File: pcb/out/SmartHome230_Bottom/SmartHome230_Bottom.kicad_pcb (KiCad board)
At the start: 2 copper layers, 120 x 92 mm, 58 parts, among them J1 B2B, J2 12V, J3 Przyciski A, J4 Przyciski B, J5 UART, J6 230V IN, J7 Wyj.1, J8 Wyj.2, K1 SRD-12V, K2 SRD-12V, Q1 BC547, Q2 BC547, SW1 EN, SW2 BOOT, U1 MP1584, U2 AMS1117-3.3, U3 ESP32-WROOM-32

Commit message: Zlicuj zlacza krawedziowe (bez zygzakow) + orientacja wejsciem do krawedzi
_place_row: zlacza I/O zlicowane zewnetrzna krawedzia ciala do brzegu plytki
(gorna krawedz rot 0, dolna strefa 230V rot 180) zamiast centrowania w pasie -
usuwa zygzaki przy krawedziach. Wnetrze (logika) nie wchodzi w pasy krawedziowe.

Co-Authored-By: Claude Opus 4.8 (1M context) <noreply@anthropic.com>
Claude-Session: https://claude.ai/code/session_01LNGxtK2Jv1rJLBLPTwFQ9C
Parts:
- moved J5 5.73 mm to (98.0, 3.27)
- moved J2 3.46 mm to (19.5, 5.54)
- moved J6 3.46 mm to (15.7, 86.5), turned to 180 degrees
- moved J7 3.46 mm to (83.5, 86.5), turned to 180 degrees
- moved J8 3.46 mm to (104.3, 86.5), turned to 180 degrees
- moved J3 2.50 mm to (44.0, 11.5)
- moved J4 2.50 mm to (70.9, 11.5)
- turned K1 to 180 degrees
- turned K2 to 180 degrees
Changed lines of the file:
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@@
     "pcbforge:ScrewTerminal_1x02_P5.08mm"
     (layer "F.Cu")
-    (at 19.5 9)
+    (at 19.5 5.54)
     (descr "Listwa zaciskowa 2x5.08mm")
     (attr through_hole)
@@
     "pcbforge:RJ45_8P8C"
     (layer "F.Cu")
-    (at 44 9)
+    (at 44 11.5)
     (descr "Gniazdo RJ45 8P8C THT")
     (attr through_hole)
@@
     "pcbforge:RJ45_8P8C"
     (layer "F.Cu")
-    (at 70.92 9)
+    (at 70.92 11.5)
     (descr "Gniazdo RJ45 8P8C THT")
     (attr through_hole)
@@
     "pcbforge:PinHeader_1x06_P2.54mm"
     (layer "F.Cu")
-    (at 97.96 9)
+    (at 97.96 3.27)
     (descr "Pin header 1x6")
     (attr through_hole)
@@
     "pcbforge:ScrewTerminal_1x03_P5.08mm"
     (layer "F.Cu")
-    (at 15.67 83)
+    (at 15.67 86.46 180)
     (descr "Listwa zaciskowa 3x5.08mm")
     (attr through_hole)
@@
     "pcbforge:Relay_SPDT_SRD"
     (layer "F.Cu")
-    (at 37.83 83)
+    (at 37.83 83 180)
     (descr "Przekaznik SRD SPDT (cewka + kontakty 230V)")
     (attr through_hole)
@@
     "pcbforge:Relay_SPDT_SRD"
     (layer "F.Cu")
-    (at 61.38 83)
+    (at 61.38 83 180)
     (descr "Przekaznik SRD SPDT (cewka + kontakty 230V)")
     (attr through_hole)
@@
     "pcbforge:ScrewTerminal_1x03_P5.08mm"
     (layer "F.Cu")
-    (at 83.55 83)
+    (at 83.55 86.46 180)
     (descr "Listwa zaciskowa 3x5.08mm")
     (attr through_hole)
@@
     "pcbforge:ScrewTerminal_1x03_P5.08mm"
     (layer "F.Cu")
-    (at 104.33 83)
+    (at 104.33 86.46 180)
     (descr "Listwa zaciskowa 3x5.08mm")
     (attr through_hole)

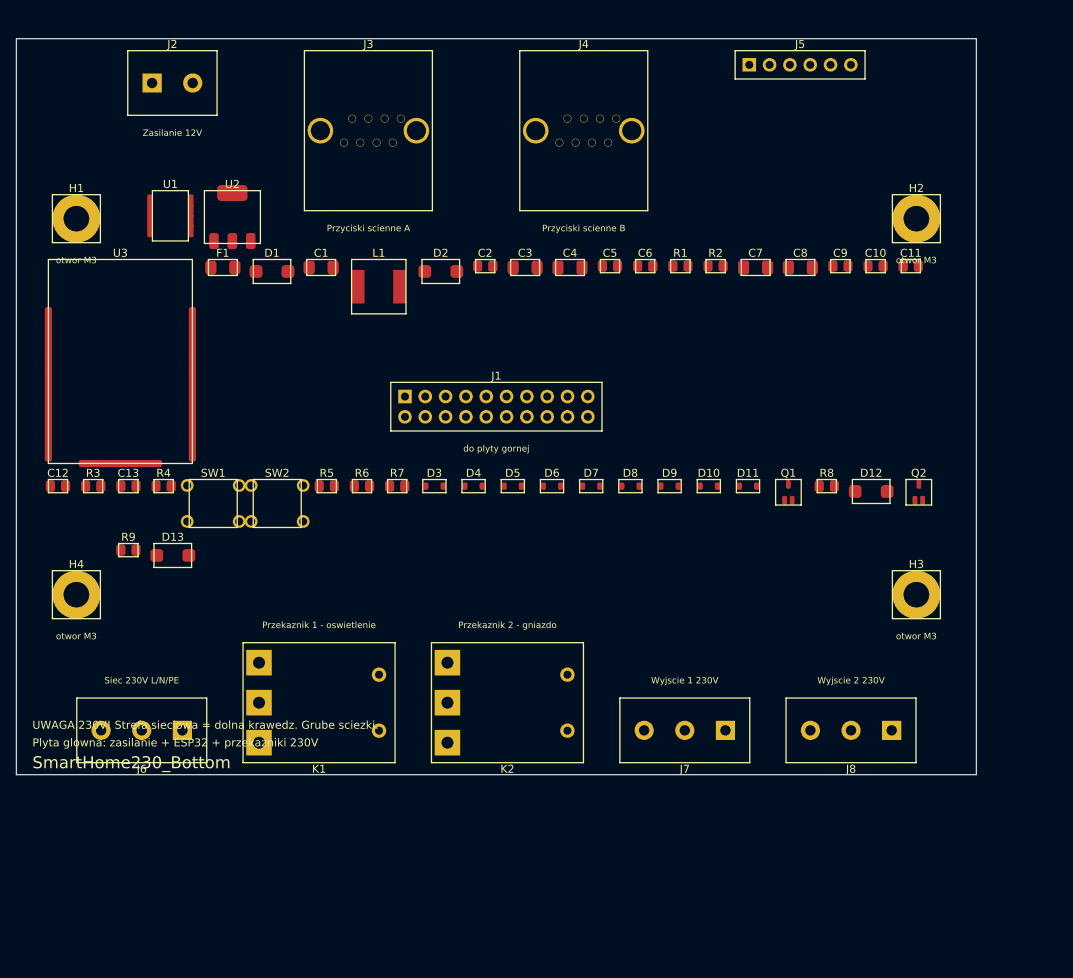
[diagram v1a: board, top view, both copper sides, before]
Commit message: Przekazniki do wnetrza (nie przy krawedzi); zaciski 230V zostaja na krawedzi
Rozdzielenie strefy 230V: zaciski sieciowe (dostep kablem) zlicowane przy dolnej
krawedzi, a przekazniki przeniesione do wnetrza w pas tuz nad zaciskami - z dala
od brzegu plytki (kolizja z obudowa). Logika pakowana nad strefa przekaznikow.
Powiekszona wspolna ramka (130x115) jako stala FRAME. SmartHome230 0/0/0, 11/11.

Co-Authored-By: Claude Opus 4.8 (1M context) <noreply@anthropic.com>
Claude-Session: https://claude.ai/code/session_01LNGxtK2Jv1rJLBLPTwFQ9C
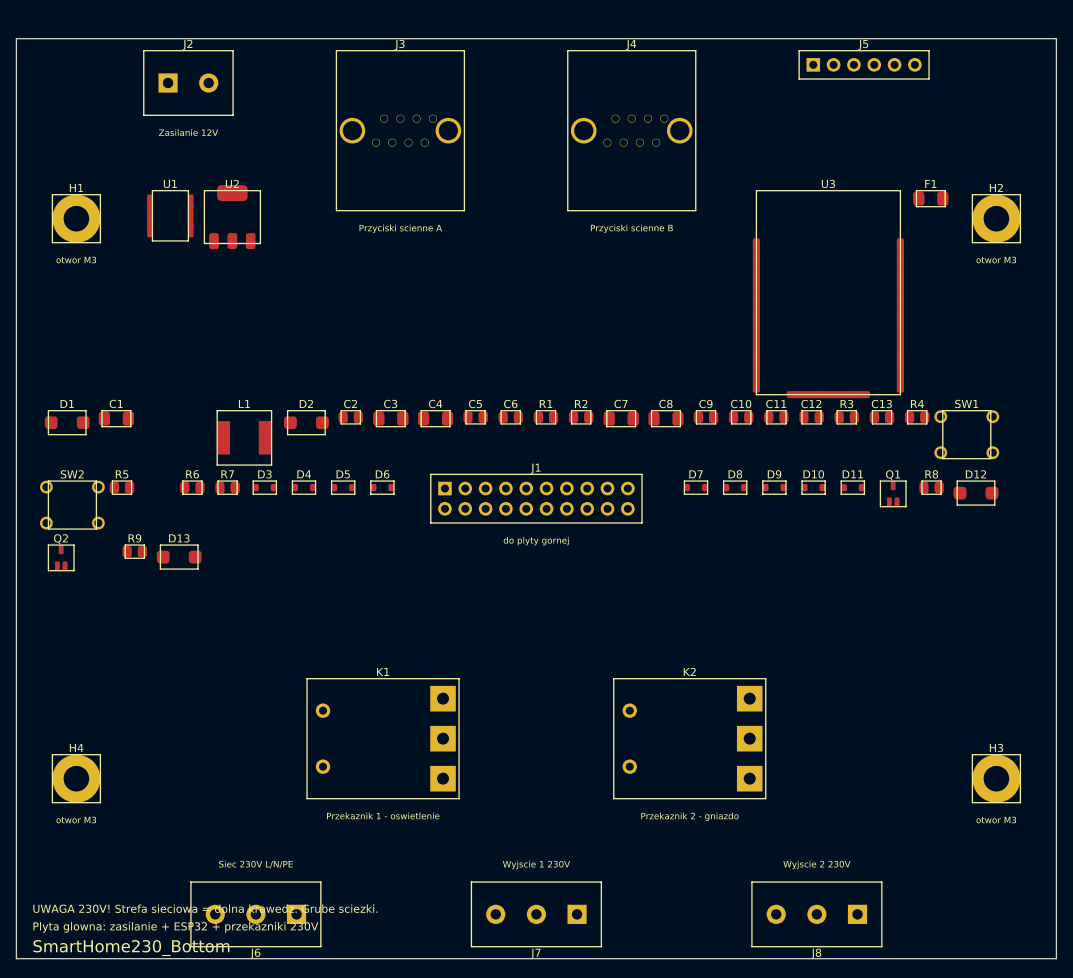
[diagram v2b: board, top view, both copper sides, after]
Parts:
- moved Q2 107.5 mm to (5.60, 64.9)
- moved C12 94.6 mm to (99.4, 47.3)
- moved C13 94.6 mm to (108.2, 47.3)
- moved R3 94.6 mm to (103.8, 47.3)
- moved R4 94.6 mm to (112.6, 47.3)
- moved SW1 94.6 mm to (118.8, 49.5)
- moved F1 88.9 mm to (114.3, 20.0)
- moved U3 88.9 mm to (101.5, 31.8)
- moved C1 31.8 mm to (12.5, 47.5)
- moved D1 31.8 mm to (6.35, 48.0)
- moved J7 29.5 mm to (65.0, 109.5)
- moved J6 27.1 mm to (29.9, 109.5)
- moved SW2 25.6 mm to (7.00, 58.3)
- moved R5 25.6 mm to (13.2, 56.1)
- moved C10 25.3 mm to (90.6, 47.3)
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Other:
- board size 120 x 92 mm -> 130 x 115 mm
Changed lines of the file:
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@@
     "pcbforge:MountingHole_M3"
     (layer "F.Cu")
-    (at 112.5 22.5)
+    (at 122.5 22.5)
     (descr "Otwor montazowy M3")
     (attr through_hole)
@@
     "pcbforge:MountingHole_M3"
     (layer "F.Cu")
-    (at 112.5 69.5)
+    (at 122.5 92.5)
     (descr "Otwor montazowy M3")
     (attr through_hole)
@@
     "pcbforge:MountingHole_M3"
     (layer "F.Cu")
-    (at 7.5 69.5)
+    (at 7.5 92.5)
     (descr "Otwor montazowy M3")
     (attr through_hole)
@@
     "pcbforge:PinHeader_2x10_P2.54mm"
     (layer "F.Cu")
-    (at 60 46)
+    (at 65 57.5)
     (descr "Pin header 2x10")
     (attr through_hole)
@@
     "pcbforge:ScrewTerminal_1x02_P5.08mm"
     (layer "F.Cu")
-    (at 19.5 5.54)
+    (at 21.5 5.54)
     (descr "Listwa zaciskowa 2x5.08mm")
     (attr through_hole)
@@
     "pcbforge:RJ45_8P8C"
     (layer "F.Cu")
-    (at 44 11.5)
+    (at 48 11.5)
     (descr "Gniazdo RJ45 8P8C THT")
     (attr through_hole)
@@
     "pcbforge:RJ45_8P8C"
     (layer "F.Cu")
-    (at 70.92 11.5)
+    (at 76.92 11.5)
     (descr "Gniazdo RJ45 8P8C THT")
     (attr through_hole)
@@
     "pcbforge:F_1206"
     (layer "F.Cu")
-    (at 25.8 28.6)
+    (at 114.3 20)
     (descr "F chip 1206")
     (attr smd)
@@
     "pcbforge:D_SMA"
     (layer "F.Cu")
-    (at 31.95 29.1)
+    (at 6.35 48)
     (descr "D_SMA")
     (attr smd)
@@
     "pcbforge:CP_1206"
     (layer "F.Cu")
-    (at 38.1 28.6)
+    (at 12.5 47.5)
     (descr "CP chip 1206")
     (attr smd)
@@
     "pcbforge:L_6x6"
     (layer "F.Cu")
-    (at 45.3 31)
+    (at 28.5 49.9)
     (descr "Cewka mocy 6x6mm")
     (attr smd)
@@
     "pcbforge:D_SMA"
     (layer "F.Cu")
-    (at 53.05 29.1)
+    (at 36.25 48)
     (descr "D_SMA")
     (attr smd)
@@
     "pcbforge:C_0805"
     (layer "F.Cu")
-    (at 58.6 28.43)
+    (at 41.8 47.33)
     (descr "C chip 0805")
     (attr smd)
@@
     "pcbforge:CP_1206"
     (layer "F.Cu")
-    (at 63.6 28.6)
+    (at 46.8 47.5)
     (descr "CP chip 1206")
     (attr smd)
@@
     "pcbforge:CP_1206"
     (layer "F.Cu")
-    (at 69.2 28.6)
+    (at 52.4 47.5)
     (descr "CP chip 1206")
     (attr smd)
@@
     "pcbforge:C_0805"
     (layer "F.Cu")
-    (at 74.2 28.43)
+    (at 57.4 47.33)
     (descr "C chip 0805")
     (attr smd)
@@
     "pcbforge:C_0805"
     (layer "F.Cu")
-    (at 78.6 28.43)
+    (at 61.8 47.33)
     (descr "C chip 0805")
     (attr smd)
@@
     "pcbforge:R_0805"
     (layer "F.Cu")
-    (at 83 28.43)
+    (at 66.2 47.33)
     (descr "R chip 0805")
     (attr smd)
@@
     "pcbforge:R_0805"
     (layer "F.Cu")
-    (at 87.4 28.43)
+    (at 70.6 47.33)
     (descr "R chip 0805")
     (attr smd)
@@
     "pcbforge:CP_1206"
     (layer "F.Cu")
-    (at 92.4 28.6)
+    (at 75.6 47.5)
     (descr "CP chip 1206")
     (attr smd)
@@
     "pcbforge:CP_1206"
     (layer "F.Cu")
-    (at 98 28.6)
+    (at 81.2 47.5)
     (descr "CP chip 1206")
     (attr smd)
@@
     "pcbforge:C_0805"
     (layer "F.Cu")
-    (at 103 28.43)
+    (at 86.2 47.33)
     (descr "C chip 0805")
     (attr smd)
@@
     "pcbforge:C_0805"
     (layer "F.Cu")
-    (at 107.4 28.43)
+    (at 90.6 47.33)
     (descr "C chip 0805")
     (attr smd)
@@
     "pcbforge:ESP32-WROOM-32"
     (layer "F.Cu")
-    (at 13 40.35)
+    (at 101.5 31.75)
     (descr "Modul ESP32-WROOM-32 (38 padow)")
     (attr smd)
@@
     "pcbforge:C_0805"
     (layer "F.Cu")
-    (at 111.8 28.43)
+    (at 95 47.33)
     (descr "C chip 0805")
     (attr smd)
@@
     "pcbforge:C_0805"
     (layer "F.Cu")
-    (at 5.2 55.93)
+    (at 99.4 47.33)
     (descr "C chip 0805")
     (attr smd)
@@
     "pcbforge:R_0805"
     (layer "F.Cu")
-    (at 9.6 55.93)
+    (at 103.8 47.33)
     (descr "R chip 0805")
     (attr smd)
@@
     "pcbforge:C_0805"
     (layer "F.Cu")
-    (at 14 55.93)
+    (at 108.2 47.33)
     (descr "C chip 0805")
     (attr smd)
@@
     "pcbforge:R_0805"
     (layer "F.Cu")
-    (at 18.4 55.93)
+    (at 112.6 47.33)
     (descr "R chip 0805")
     (attr smd)
@@
     "pcbforge:SW_Push_6mm"
     (layer "F.Cu")
-    (at 24.6 58.1)
+    (at 118.8 49.5)
     (descr "Tact switch 6mm")
     (attr through_hole)
@@
     "pcbforge:SW_Push_6mm"
     (layer "F.Cu")
-    (at 32.6 58.1)
+    (at 7 58.3)
     (descr "Tact switch 6mm")
     (attr through_hole)
@@
     "pcbforge:PinHeader_1x06_P2.54mm"
     (layer "F.Cu")
-    (at 97.96 3.27)
+    (at 105.96 3.27)
     (descr "Pin header 1x6")
     (attr through_hole)
@@
     "pcbforge:R_0805"
     (layer "F.Cu")
-    (at 38.8 55.93)
+    (at 13.2 56.12)
     (descr "R chip 0805")
     (attr smd)
@@
     "pcbforge:R_0805"
     (layer "F.Cu")
-    (at 43.2 55.93)
+    (at 22 56.12)
     (descr "R chip 0805")
     (attr smd)
@@
     "pcbforge:R_0805"
     (layer "F.Cu")
-    (at 47.6 55.93)
+    (at 26.4 56.12)
     (descr "R chip 0805")
     (attr smd)
@@
     "pcbforge:D_SOD-323"
     (layer "F.Cu")
-    (at 52.25 55.93)
+    (at 31.05 56.12)
     (descr "D_SOD-323")
     (attr smd)
@@
     "pcbforge:D_SOD-323"
     (layer "F.Cu")
-    (at 57.15 55.93)
+    (at 35.95 56.12)
     (descr "D_SOD-323")
     (attr smd)
@@
     "pcbforge:D_SOD-323"
     (layer "F.Cu")
-    (at 62.05 55.93)
+    (at 40.85 56.12)
     (descr "D_SOD-323")
     (attr smd)
@@
     "pcbforge:D_SOD-323"
     (layer "F.Cu")
-    (at 66.95 55.93)
+    (at 45.75 56.12)
     (descr "D_SOD-323")
     (attr smd)
@@
     "pcbforge:D_SOD-323"
     (layer "F.Cu")
-    (at 71.85 55.93)
+    (at 84.95 56.12)
     (descr "D_SOD-323")
     (attr smd)
@@
     "pcbforge:D_SOD-323"
     (layer "F.Cu")
-    (at 76.75 55.93)
+    (at 89.85 56.12)
     (descr "D_SOD-323")
     (attr smd)
@@
     "pcbforge:D_SOD-323"
     (layer "F.Cu")
-    (at 81.65 55.93)
+    (at 94.75 56.12)
     (descr "D_SOD-323")
     (attr smd)
@@
     "pcbforge:D_SOD-323"
     (layer "F.Cu")
-    (at 86.55 55.93)
+    (at 99.65 56.12)
     (descr "D_SOD-323")
     (attr smd)
@@
     "pcbforge:D_SOD-323"
     (layer "F.Cu")
-    (at 91.45 55.93)
+    (at 104.55 56.12)
     (descr "D_SOD-323")
     (attr smd)
@@
     "pcbforge:ScrewTerminal_1x03_P5.08mm"
     (layer "F.Cu")
-    (at 15.67 86.46 180)
+    (at 29.94 109.46 180)
     (descr "Listwa zaciskowa 3x5.08mm")
     (attr through_hole)
@@
     "pcbforge:Relay_SPDT_SRD"
     (layer "F.Cu")
-    (at 37.83 83 180)
+    (at 45.83 87.5)
     (descr "Przekaznik SRD SPDT (cewka + kontakty 230V)")
     (attr through_hole)
@@
     "pcbforge:SOT-23-3"
     (layer "F.Cu")
-    (at 96.5 56.7)
+    (at 109.6 56.9)
     (descr "SOT-23-3")
     (attr smd)
@@
     "pcbforge:R_0805"
     (layer "F.Cu")
-    (at 101.3 55.93)
+    (at 114.4 56.12)
     (descr "R chip 0805")
     (attr smd)
@@
     "pcbforge:D_SMA"
     (layer "F.Cu")
-    (at 106.85 56.6)
+    (at 119.95 56.8)
     (descr "D_SMA")
     (attr smd)
@@
     "pcbforge:Relay_SPDT_SRD"
     (layer "F.Cu")
-    (at 61.38 83 180)
+    (at 84.17 87.5)
     (descr "Przekaznik SRD SPDT (cewka + kontakty 230V)")
     (attr through_hole)
@@
     "pcbforge:SOT-23-3"
     (layer "F.Cu")
-    (at 112.8 56.7)
+    (at 5.6 64.9)
     (descr "SOT-23-3")
     (attr smd)
@@
     "pcbforge:R_0805"
     (layer "F.Cu")
-    (at 14 63.93)
+    (at 14.8 64.12)
     (descr "R chip 0805")
     (attr smd)
@@
     "pcbforge:D_SMA"
     (layer "F.Cu")
-    (at 19.55 64.6)
+    (at 20.35 64.8)
     (descr "D_SMA")
     (attr smd)
@@
     "pcbforge:ScrewTerminal_1x03_P5.08mm"
     (layer "F.Cu")
-    (at 83.55 86.46 180)
+    (at 65 109.46 180)
     (descr "Listwa zaciskowa 3x5.08mm")
     (attr through_hole)
@@
     "pcbforge:ScrewTerminal_1x03_P5.08mm"
     (layer "F.Cu")
-    (at 104.33 86.46 180)
+    (at 100.06 109.46 180)
     (descr "Listwa zaciskowa 3x5.08mm")
     (attr through_hole)
@@
   (gr_line
     (start 0 0)
-    (end 120 0)
+    (end 130 0)
     (stroke
       (width 0.1)
@@
   )
   (gr_line
-    (start 120 0)
-    (end 120 92)
+    (start 130 0)
+    (end 130 115)
     (stroke
       (width 0.1)
@@
   )
   (gr_line
-    (start 120 92)
-    (end 0 92)
+    (start 130 115)
+    (end 0 115)
     (stroke
       (width 0.1)
@@
   )
   (gr_line
-    (start 0 92)
+    (start 0 115)
     (end 0 0)
     (stroke
@@
   (gr_text
     "SmartHome230_Bottom"
-    (at 2 90.5 0)
+    (at 2 113.5 0)
     (layer "F.SilkS")
     (effects
@@
   (gr_text
     "Plyta glowna: zasilanie + ESP32 + przekazniki 230V"
-    (at 2 88 0)
+    (at 2 111 0)
     (layer "F.SilkS")
     (effects
@@
   (gr_text
     "UWAGA 230V! Strefa sieciowa = dolna krawedz. Grube sciezki."
-    (at 2 85.8 0)
+    (at 2 108.8 0)
     (layer "F.SilkS")
     (effects
